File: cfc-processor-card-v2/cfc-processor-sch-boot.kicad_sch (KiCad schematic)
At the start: 22 parts, among them J3 CONN_03LONGPADS, U7 OSD3358-512M-BSM

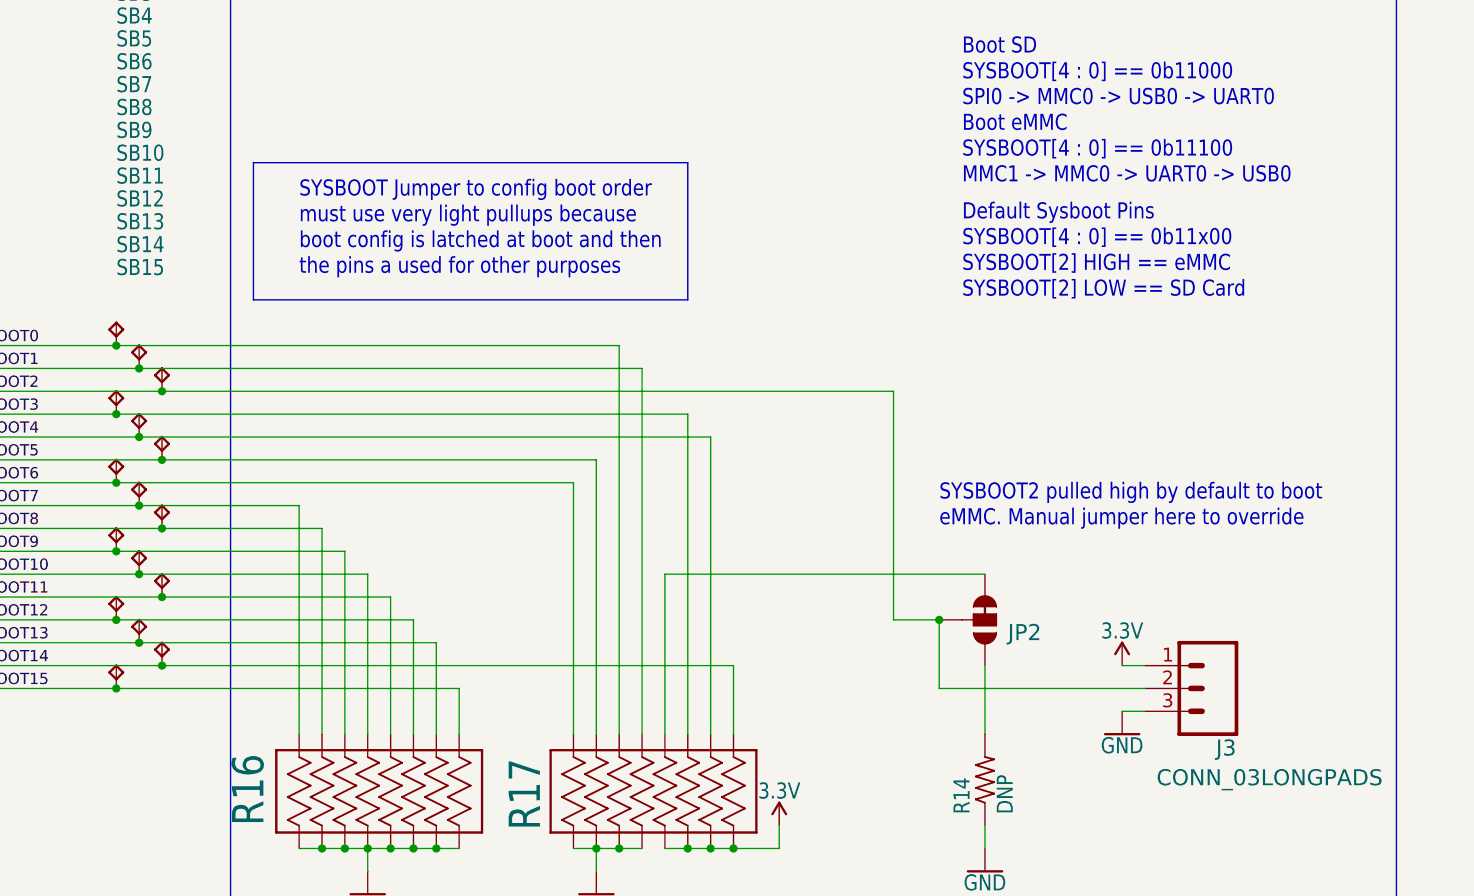
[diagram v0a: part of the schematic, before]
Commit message: Big cleanup - fixed a billion ERCs and DRCs. Switched a bunch of parts over to OreSat parts. Added analog switch on UART so CFC processor can talk serial to C3. Last thing left: clean up passives with new footprints, maybe.
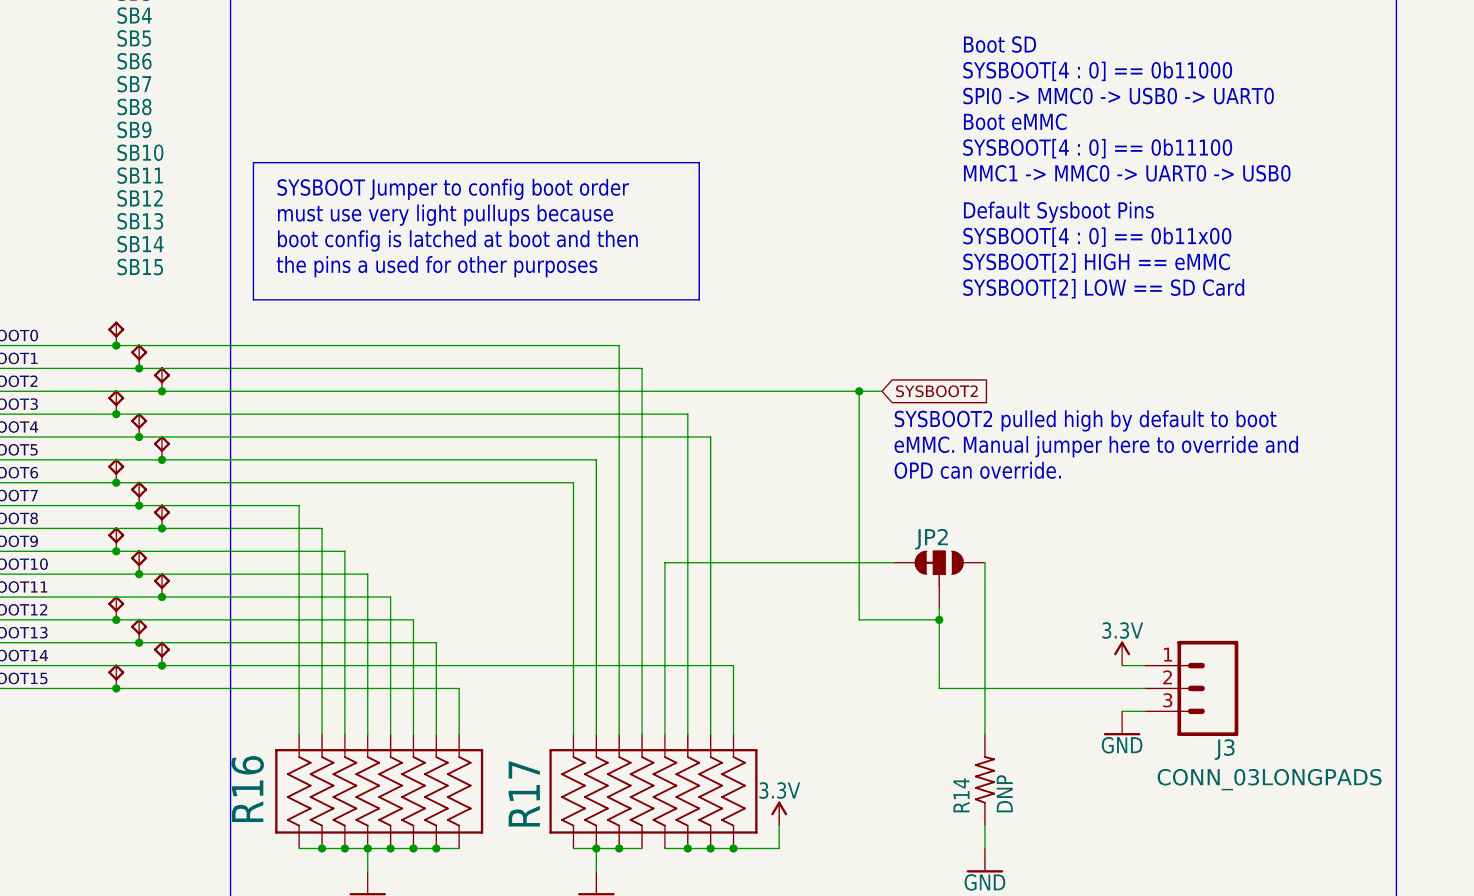
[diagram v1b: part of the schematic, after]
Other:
- note added: "SYSBOOT2 pulled high by default to boot eMMC. Manual jumper here to override and OPD can override."
- note removed: "SYSBOOT2 pulled high by default to boot eMMC. Manual jumper here to override"
- moved on the sheet: JP2
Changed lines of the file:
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@@
 	(text "SYSBOOT Jumper to config boot order\nmust use very light pullups because\nboot config is latched at boot and then\nthe pins a used for other purposes"
 		(exclude_from_sim no)
-		(at 205.74 99.06 0)
+		(at 203.2 99.06 0)
 		(effects
 			(font
@@
 		)
 	)
-	(text "SYSBOOT2 pulled high by default to boot\neMMC. Manual jumper here to override"
+	(text "SYSBOOT2 pulled high by default to boot\neMMC. Manual jumper here to override and\nOPD can override."
 		(exclude_from_sim no)
-		(at 276.86 127 0)
+		(at 271.78 121.92 0)
 		(effects
 			(font
@@
 	)
 	(junction
+		(at 267.97 111.76)
+		(diameter 0)
+		(color 0 0 0 0)
+	)
+	(junction
 		(at 185.42 129.54)
 		(diameter 0)
@@
 	(wire
 		(pts
-			(xy 281.94 132.08) (xy 246.38 132.08)
-		)
-		(stroke
-			(width 0.1524)
-			(type solid)
-		)
-	)
-	(wire
-		(pts
 			(xy 208.28 162.56) (xy 210.82 162.56)
 		)
@@
 	(wire
 		(pts
-			(xy 190.5 111.76) (xy 271.78 111.76)
+			(xy 190.5 111.76) (xy 267.97 111.76)
 		)
 		(stroke
@@
 	(wire
 		(pts
-			(xy 281.94 142.24) (xy 281.94 149.86)
+			(xy 281.94 130.81) (xy 281.94 149.86)
 		)
 		(stroke
@@
 	(wire
 		(pts
-			(xy 271.78 111.76) (xy 271.78 137.16)
+			(xy 267.97 111.76) (xy 267.97 137.16)
 		)
 		(stroke
@@
 	(polyline
 		(pts
-			(xy 248.92 101.6) (xy 248.92 86.36)
+			(xy 250.19 101.6) (xy 250.19 86.36)
 		)
 		(stroke
@@
 	(wire
 		(pts
-			(xy 276.86 137.16) (xy 271.78 137.16)
-		)
-		(stroke
-			(width 0.1524)
-			(type solid)
+			(xy 276.86 137.16) (xy 267.97 137.16)
+		)
+		(stroke
+			(width 0.1524)
+			(type solid)
+		)
+	)
+	(wire
+		(pts
+			(xy 267.97 111.76) (xy 270.51 111.76)
+		)
+		(stroke
+			(width 0)
+			(type default)
 		)
 	)
@@
 	(wire
 		(pts
+			(xy 246.38 130.81) (xy 271.78 130.81)
+		)
+		(stroke
+			(width 0.1524)
+			(type solid)
+		)
+	)
+	(wire
+		(pts
 			(xy 218.44 149.86) (xy 218.44 137.16)
 		)
@@
 	(wire
 		(pts
-			(xy 246.38 132.08) (xy 246.38 149.86)
-		)
-		(stroke
-			(width 0.1524)
-			(type solid)
-		)
-	)
-	(wire
-		(pts
 			(xy 162.56 144.78) (xy 185.42 144.78)
 		)
@@
 	(polyline
 		(pts
-			(xy 248.92 86.36) (xy 200.66 86.36)
+			(xy 250.19 86.36) (xy 200.66 86.36)
 		)
 		(stroke
@@
 	(wire
 		(pts
+			(xy 246.38 130.81) (xy 246.38 149.86)
+		)
+		(stroke
+			(width 0.1524)
+			(type solid)
+		)
+	)
+	(wire
+		(pts
+			(xy 276.86 135.89) (xy 276.86 137.16)
+		)
+		(stroke
+			(width 0)
+			(type default)
+		)
+	)
+	(wire
+		(pts
 			(xy 213.36 162.56) (xy 215.9 162.56)
 		)
@@
 	(polyline
 		(pts
-			(xy 200.66 101.6) (xy 248.92 101.6)
+			(xy 200.66 101.6) (xy 250.19 101.6)
 		)
 		(stroke
@@
 			)
 			(justify left bottom)
+		)
+	)
+	(global_label "SYSBOOT2"
+		(shape input)
+		(at 270.51 111.76 0)
+		(fields_autoplaced yes)
+		(effects
+			(font
+				(size 1.27 1.27)
+			)
+			(justify left)
+		)
+		(property "Intersheetrefs" "${INTERSHEET_REFS}"
+			(at 283.1109 111.76 0)
+			(effects
+				(font
+					(size 1.27 1.27)
+				)
+				(justify left)
+			)
 		)
 	)
@@
 				)
 				(justify right)
-				(hide yes)
 			)
 		)
@@
 				)
 				(justify right)
-				(hide yes)
 			)
 		)
@@
 	(symbol
 		(lib_id "cfc-card-eagle-import:JUMPER-SMT_3_1-NC_TRACE_SILK")
-		(at 281.94 137.16 0)
+		(at 276.86 130.81 270)
 		(mirror x)
 		(unit 1)
@@
 		(dnp no)
 		(property "Reference" "JP2"
-			(at 284.48 137.541 0)
+			(at 274.32 127 90)
 			(effects
 				(font
@@
 		)
 		(property "Value" "JUMPER-SMT_3_1-NC_TRACE_SILK"
-			(at 284.48 136.779 0)
+			(at 276.479 128.27 0)
 			(effects
 				(font
@@
 		)
 		(property "Footprint" "cfc-card:SMT-JUMPER_3_1-NC_TRACE_SILK"
-			(at 281.94 137.16 0)
+			(at 276.86 130.81 0)
 			(effects
 				(font
@@
 		)
 		(property "Datasheet" ""
-			(at 281.94 137.16 0)
+			(at 276.86 130.81 0)
 			(effects
 				(font
@@
 		)
 		(property "Description" ""
-			(at 281.94 137.16 0)
-			(effects
-				(font
+			(at 276.86 130.81 0)
+			(effects
+				(font

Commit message: more trace polishing.
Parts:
- R14: footprint cfc-card:.0603-A -> oresat-passives:0603-C-NOSILK
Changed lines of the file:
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@@
 			)
 		)
-		(property "Footprint" "cfc-card:.0603-A"
+		(property "Footprint" "oresat-passives:0603-C-NOSILK"
 			(at 281.94 154.94 0)
 			(effects

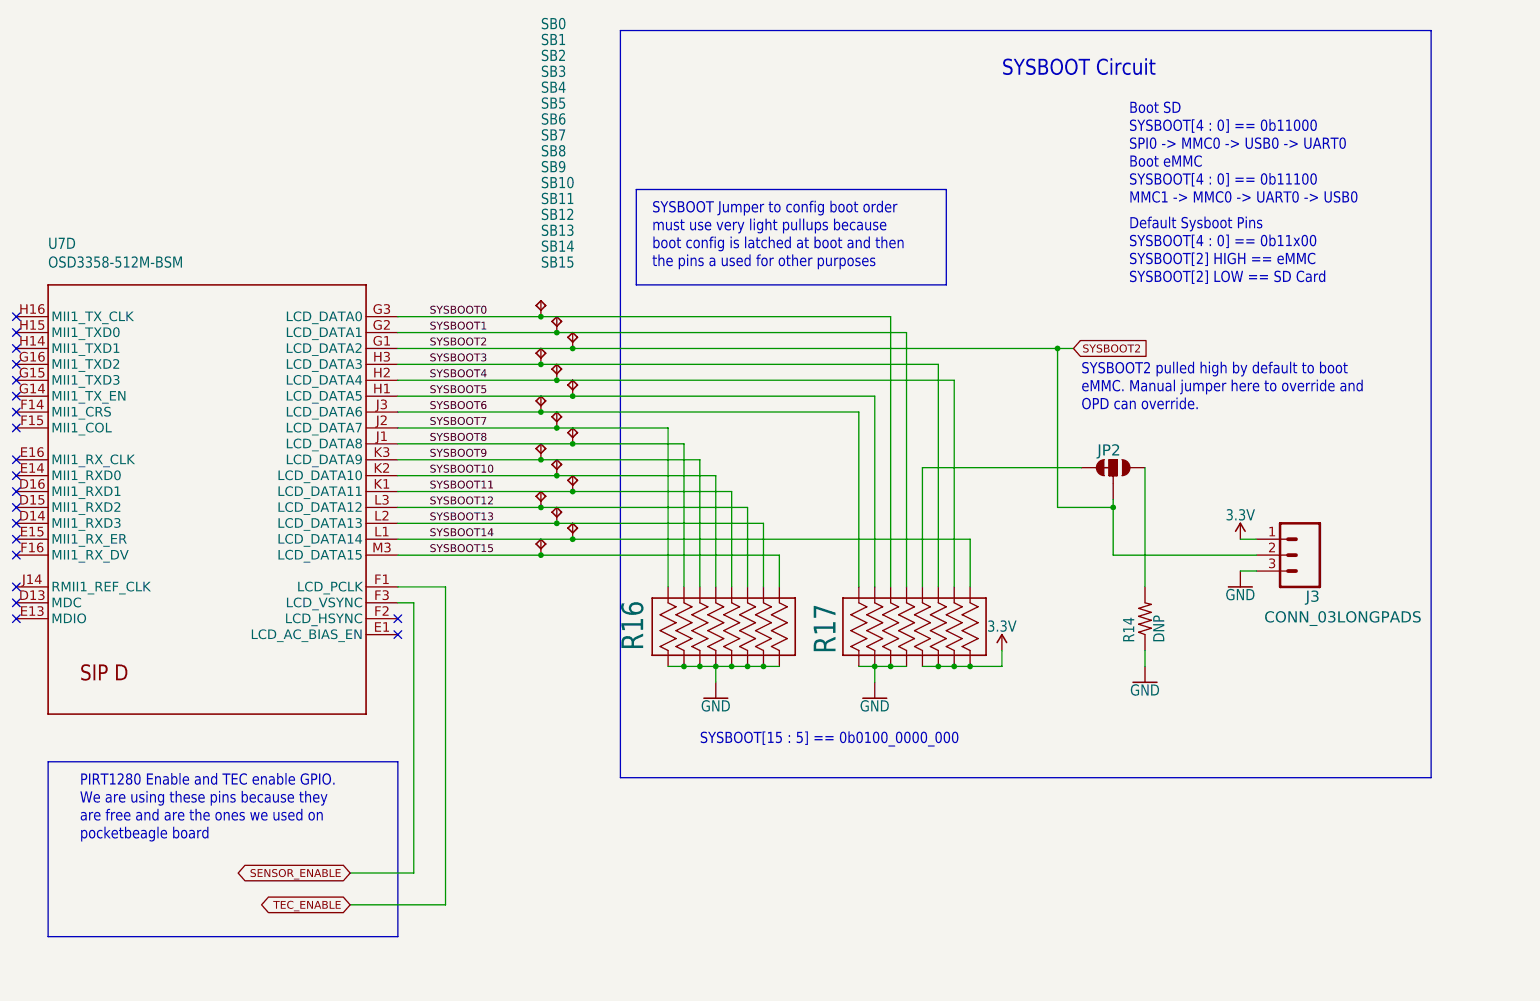
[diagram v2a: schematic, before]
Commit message: Final polish on schematic and PCB. Cleaned up BOM, fixed github issues which were not really issues. Lots of BOM cleanup, with MPNs and DPNs.
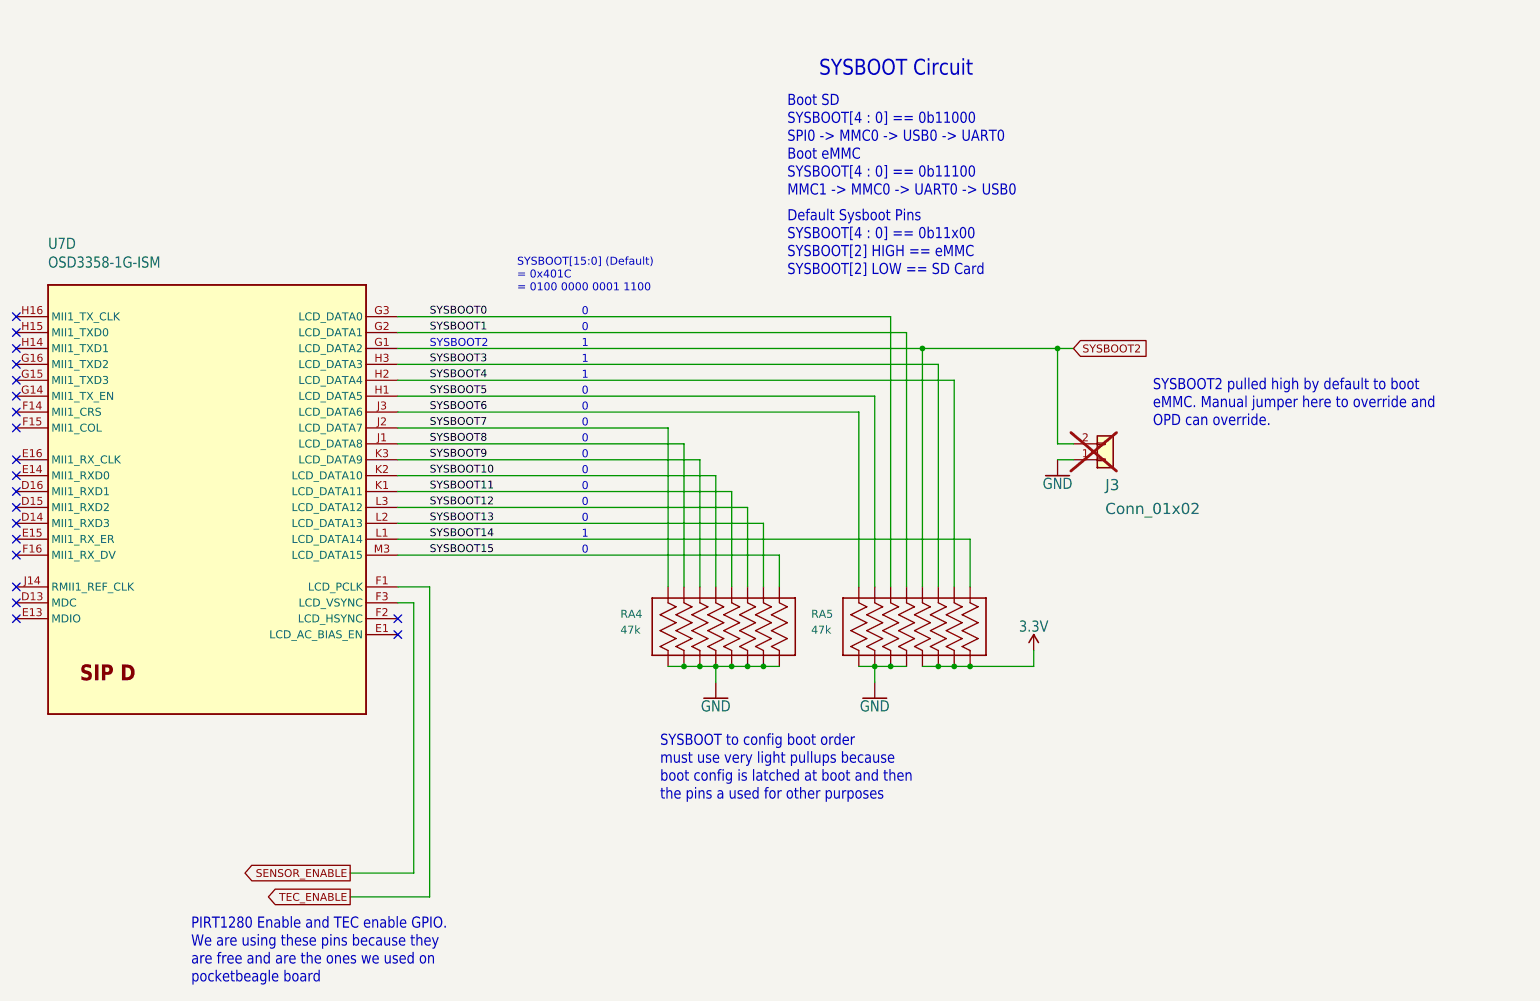
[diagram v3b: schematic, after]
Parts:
- removed JP2: JUMPER-SMT_3_1-NC_TRACE_SILK, cfc-card:SMT-JUMPER_3_1-NC_TRACE_SILK, symbol cfc-card-eagle-import:JUMPER-SMT_3_1-NC_TRACE_SILK
- removed R14: DNP, oresat-passives:0603-C-NOSILK, symbol cfc-card-eagle-import:R-US_0603-A
- removed SB0, SB1, SB10, SB11, SB12, SB13, SB14, SB15, SB2, SB3, SB4, SB5, SB6, SB7, SB8, SB9: TEST-POINT-SMALL, cfc-card:TEST-POINT-SMALL, symbol cfc-card-eagle-import:TEST-POINT-SMALL
- J3: value CONN_03LONGPADS -> Conn_01x02; footprint cfc-card:1X03_LONGPADS -> Connector_PinHeader_2.54mm:PinHeader_1x02_P2.54mm_Vertical; symbol cfc-card-eagle-import:CONN_03LONGPADS -> Connector_Generic:Conn_01x02; now not fitted
- RA4: renamed from R16; value 100k -> 47k; DIS (none) -> DigiKey; DPN (none) -> Y1473CT-ND; MFR (none) -> 47k Ohm ±5% 62.5mW Power Per Element Isolated 8 Resistor Ne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; MPN (none) -> EXB-2HV473JV
- RA5: renamed from R17; value 100k -> 47k; DIS (none) -> DigiKey; DPN (none) -> Y1473CT-ND; MFR (none) -> 47k Ohm ±5% 62.5mW Power Per Element Isolated 8 Resistor Ne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; MPN (none) -> EXB-2HV473JV
- U7: value OSD3358-512M-BSM -> OSD3358-1G-ISM; footprint cfc-card:OSD335X-BGA-256 -> oresat-ics:U-Octavo-OSD335X-BGA-256; symbol cfc-card-eagle-import:OSD3358-512M-BSM -> oresat-ics:OSD3358-512M-BSM; DIS (none) -> DigiKey; DPN (none) -> 1676-OSD3358-1G-ISM-ND; MFR (none) -> Octavo Systems; MPN (none) -> OSD3358-1G-ISM
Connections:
- net 3.3V: no longer J3.1
- net GND: now also J3.1 (Pin_1); no longer J3.3
- net SYSBOOT2: now also RA5.12
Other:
- note added: "0"
- note added: "1"
- note added: "SYSBOOT to config boot order must use very light pullups because boot config is latched at boot and then the pins a used for other purposes"
- note added: "SYSBOOT2"
- note added: "SYSBOOT[15:0] (Default) = 0x401C = 0100 0000 0001 1100"
- note removed: "SYSBOOT Jumper to config boot order must use very light pullups because boot config is latched at boot and then the pins a used for other purposes"
- note removed: "SYSBOOT[15 : 5] == 0b0100_0000_000"
